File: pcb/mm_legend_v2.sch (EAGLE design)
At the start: 74 parts, among them IC1 ULN2003AD, IC2 TB6612FNG

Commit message: pcb: created pcb design.
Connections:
- net +5V/1 renamed 3V3
- net +5V/2 renamed AVDD
- removed net N$26: IC2.AO1@2
- removed net N$27: IC2.AO2@1, MOTOR1.5
- removed net N$29: IC2.BO1@1, MOTOR2.6
- net IR_DIAG_L: now also IC1.I2, STM1PORT_C_L.PC05; no longer IC1.I4, STM1PORT_C_L.PC03
- net IR_DIAG_R: now also IC1.I5, STM1PORT_C_L.PC01; no longer IC1.I3, STM1PORT_C_L.PC02
- net IR_FRONT_L: now also IC1.I1, STM1PORT_C_L.PC04; no longer IC1.I2, STM1PORT_C_L.PC01
- net IR_FRONT_R: now also IC1.I6; no longer IC1.I1
- net IR_SIDE_L: now also IC1.I3, STM1PORT_C_L.PC03; no longer IC1.I6, STM1PORT_C_L.PC05
- net IR_SIDE_R: now also IC1.I4, STM1PORT_C_L.PC02; no longer IC1.I5, STM1PORT_C_L.PC04
- net MOTOR1_CH1: now also STM1PORT_C_L.PC07; no longer STM1PORT_C_L.PC06
- net MOTOR1_CH2: now also STM1PORT_C_L.PC06; no longer STM1PORT_C_L.PC07
- net MOTOR1_PWM: now also STM1PORT_A_L.PA01; no longer STM1PORT_A_L.PA00
- net MOTOR2_PWM: now also STM1PORT_A_L.PA00; no longer STM1PORT_A_L.PA01
- net N$10: now also IR_DIAG_L.C, R11.2; no longer IR_SIDE_R.C, R14.2
- net N$11: now also IR_SIDE_L.C, R12.2; no longer IR_DIAG_L.C, R13.2
- net N$12: now also IR_SIDE_R.C, R13.2; no longer IR_DIAG_R.C, R12.2
- net N$13: now also IR_DIAG_R.C, R14.2; no longer IR_FRONT_L.C, R11.2
- net N$14: now also R15.2; no longer R10.2
- net N$23: now also IC2.AO1@2, MOTOR1.5; no longer MOTOR1.6
- net N$24: now also IC2.AO2@1, MOTOR1.6
- net N$28: now also IC2.BO1@1, MOTOR2.6
- net N$8: now also IR_FRONT_L.C, R10.2; no longer IR_SIDE_L.C, R15.2
- net PHOTO_DIAG_L: now also STM1PORT_A_L.PA06; no longer STM1PORT_A_L.PA05
- net PHOTO_DIAG_R: now also STM1PORT_A_L.PA03; no longer STM1PORT_A_L.PA04
- net PHOTO_FRONT_L: now also STM1PORT_A_L.PA07; no longer STM1PORT_A_L.PA03
- net PHOTO_SIDE_L: now also STM1PORT_A_L.PA05; no longer STM1PORT_A_L.PA07
- net PHOTO_SIDE_R: now also STM1PORT_A_L.PA04; no longer STM1PORT_A_L.PA06
- net SW1: now also STM1PORT_B_L.PB01; no longer STM1PORT_C_H.PC10
- net SW2: now also STM1PORT_B_L.PB02; no longer STM1PORT_C_H.PC11
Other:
- moved on the sheet: IR_DIAG_L, IR_DIAG_R, IR_FRONT_L, IR_FRONT_R, IR_SIDE_L, IR_SIDE_R

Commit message: pcb: minor changes in pcb and schematic.
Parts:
- C17: value 100u -> 100n
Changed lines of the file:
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@@
 <part name="SUPPLY21" library="supply2" deviceset="VCC" device=""/>
 <part name="SUPPLY22" library="supply2" deviceset="+5V/1" device="" value="3V3"/>
-<part name="C17" library="resistor" deviceset="C-EU" device="C0805K" value="100u"/>
+<part name="C17" library="resistor" deviceset="C-EU" device="C0805K" value="100n"/>
 <part name="R17" library="resistor" deviceset="R-EU_" device="R0805W" value="10k"/>
 <part name="SUPPLY23" library="supply2" deviceset="+5V/1" device="" value="3V3"/>

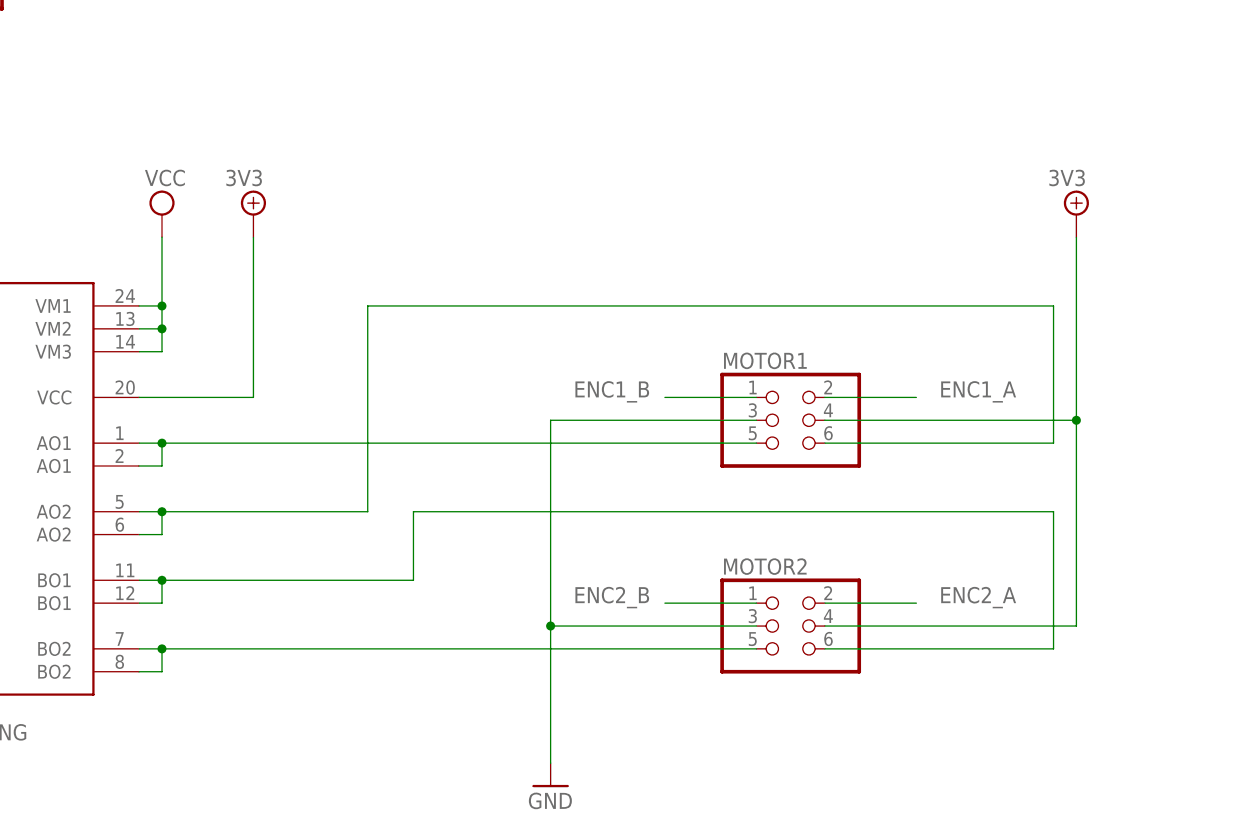
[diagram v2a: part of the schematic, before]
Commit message: pcb: update pcb and schematic.
Changes:
- Moved BT connector away from motor holder.
- Changed pinout of motor connectors - fix issue #1.
- Added thicker lines for motor + and - signals.
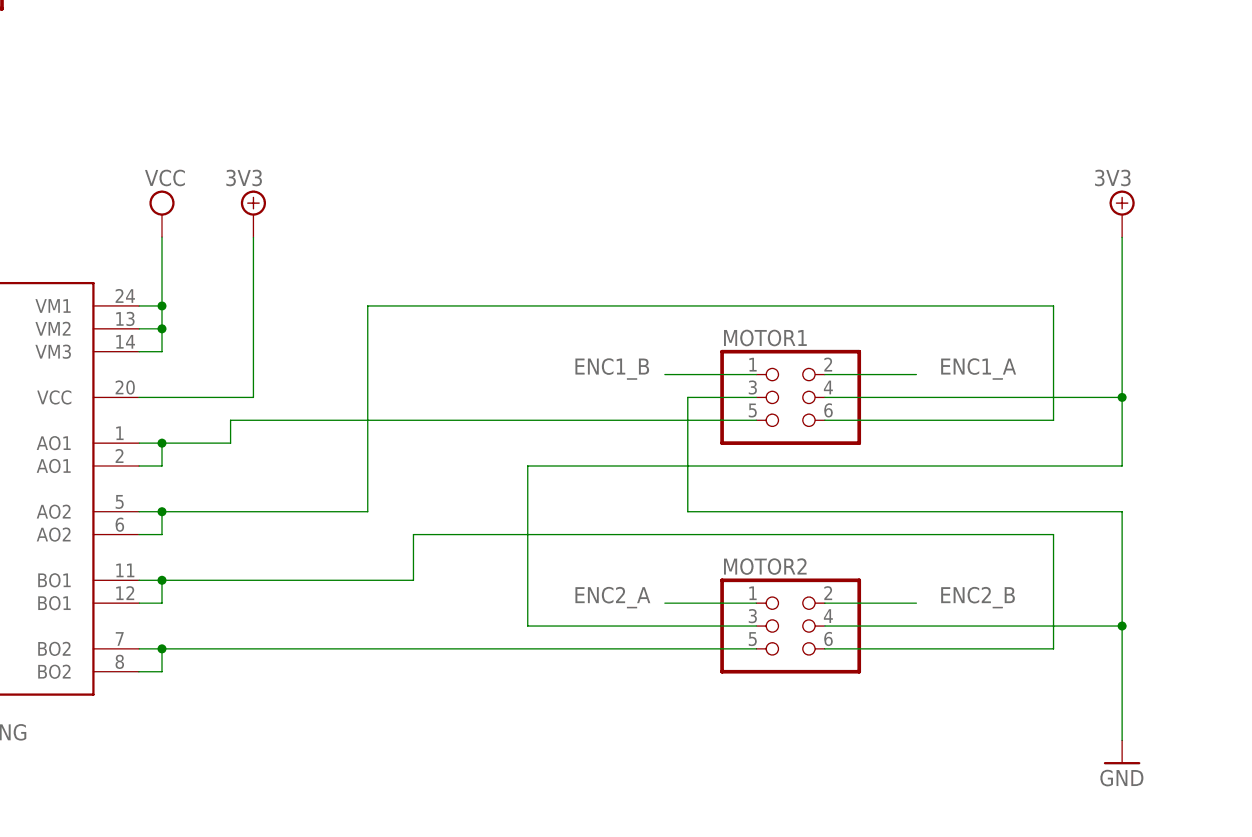
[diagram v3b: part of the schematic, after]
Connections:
- net 3V3: now also MOTOR2.3; no longer MOTOR2.4
- net ENC2_A: now also MOTOR2.1; no longer MOTOR2.2
- net ENC2_B: now also MOTOR2.2; no longer MOTOR2.1
- net GND: now also MOTOR2.4; no longer MOTOR2.3
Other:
- moved on the sheet: MOTOR1
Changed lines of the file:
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@@
 <part name="MOTOR2" library="pinhead" deviceset="PINHD-2X3" device=""/>
 <part name="GND25" library="supply1" deviceset="GND" device=""/>
-<part name="SUPPLY26" library="supply2" deviceset="+5V/1" device="" value="3V3"/>
 <part name="PHOTO_FRONT_R" library="photo_transistor_5mm" deviceset="PHOTO_TRANSISTOR_5MM" device="" value=""/>
 <part name="PHOTO_FRONT_L" library="photo_transistor_5mm" deviceset="PHOTO_TRANSISTOR_5MM" device="" value=""/>
@@
 <part name="SUPPLY31" library="supply2" deviceset="+5V/2" device="" value="AVDD"/>
 <part name="SUPPLY32" library="supply2" deviceset="+5V/2" device="" value="AVDD"/>
+<part name="SUPPLY26" library="supply2" deviceset="+5V/1" device="" value="3V3"/>
 </parts>
 <sheets>
@@
 <instance part="SUPPLY25" gate="G$1" x="208.28" y="-22.86"/>
 <instance part="GND24" gate="1" x="208.28" y="-45.72"/>
-<instance part="MOTOR1" gate="A" x="337.82" y="-5.08"/>
+<instance part="MOTOR1" gate="A" x="337.82" y="-2.54"/>
 <instance part="MOTOR2" gate="A" x="337.82" y="-27.94"/>
-<instance part="GND25" gate="1" x="312.42" y="-45.72"/>
-<instance part="SUPPLY26" gate="G$1" x="370.84" y="17.78"/>
+<instance part="GND25" gate="1" x="375.92" y="-43.18"/>
 <instance part="PHOTO_FRONT_R" gate="G$1" x="190.5" y="144.78"/>
 <instance part="PHOTO_FRONT_L" gate="G$1" x="226.06" y="144.78"/>
@@
 <instance part="SUPPLY31" gate="G$1" x="330.2" y="157.48"/>
 <instance part="SUPPLY32" gate="G$1" x="365.76" y="157.48"/>
+<instance part="SUPPLY26" gate="G$1" x="375.92" y="17.78"/>
 </instances>
 <busses>
@@
 </segment>
 <segment>
-<pinref part="GND25" gate="1" pin="GND"/>
-<wire x1="312.42" y1="-43.18" x2="312.42" y2="-27.94" width="0.1524" layer="91"/>
-<pinref part="MOTOR2" gate="A" pin="3"/>
-<wire x1="312.42" y1="-27.94" x2="335.28" y2="-27.94" width="0.1524" layer="91"/>
-<wire x1="312.42" y1="-27.94" x2="312.42" y2="-5.08" width="0.1524" layer="91"/>
-<pinref part="MOTOR1" gate="A" pin="3"/>
-<wire x1="312.42" y1="-5.08" x2="335.28" y2="-5.08" width="0.1524" layer="91"/>
-<junction x="312.42" y="-27.94"/>
-</segment>
-<segment>
 <pinref part="GND26" gate="1" pin="GND"/>
 <pinref part="R18" gate="G$1" pin="1"/>
@@
 <pinref part="R23" gate="G$1" pin="1"/>
 <wire x1="365.76" y1="119.38" x2="365.76" y2="124.46" width="0.1524" layer="91"/>
+</segment>
+<segment>
+<pinref part="MOTOR2" gate="A" pin="4"/>
+<pinref part="GND25" gate="1" pin="GND"/>
+<wire x1="342.9" y1="-27.94" x2="375.92" y2="-27.94" width="0.1524" layer="91"/>
+<wire x1="375.92" y1="-27.94" x2="375.92" y2="-40.64" width="0.1524" layer="91"/>
+<wire x1="375.92" y1="-27.94" x2="375.92" y2="-15.24" width="0.1524" layer="91"/>
+<wire x1="375.92" y1="-15.24" x2="327.66" y2="-15.24" width="0.1524" layer="91"/>
+<wire x1="327.66" y1="-15.24" x2="327.66" y2="-2.54" width="0.1524" layer="91"/>
+<pinref part="MOTOR1" gate="A" pin="3"/>
+<wire x1="327.66" y1="-2.54" x2="335.28" y2="-2.54" width="0.1524" layer="91"/>
+<junction x="375.92" y="-27.94"/>
 </segment>
 </net>
@@
 <segment>
 <pinref part="SUPPLY26" gate="G$1" pin="+5V/1"/>
-<wire x1="370.84" y1="15.24" x2="370.84" y2="-5.08" width="0.1524" layer="91"/>
+<wire x1="375.92" y1="15.24" x2="375.92" y2="-2.54" width="0.1524" layer="91"/>
 <pinref part="MOTOR1" gate="A" pin="4"/>
-<wire x1="370.84" y1="-5.08" x2="342.9" y2="-5.08" width="0.1524" layer="91"/>
-<wire x1="370.84" y1="-5.08" x2="370.84" y2="-27.94" width="0.1524" layer="91"/>
-<pinref part="MOTOR2" gate="A" pin="4"/>
-<wire x1="370.84" y1="-27.94" x2="342.9" y2="-27.94" width="0.1524" layer="91"/>
-<junction x="370.84" y="-5.08"/>
+<wire x1="375.92" y1="-2.54" x2="342.9" y2="-2.54" width="0.1524" layer="91"/>
+<pinref part="MOTOR2" gate="A" pin="3"/>
+<wire x1="335.28" y1="-27.94" x2="309.88" y2="-27.94" width="0.1524" layer="91"/>
+<wire x1="309.88" y1="-27.94" x2="309.88" y2="-10.16" width="0.1524" layer="91"/>
+<wire x1="309.88" y1="-10.16" x2="375.92" y2="-10.16" width="0.1524" layer="91"/>
+<wire x1="375.92" y1="-10.16" x2="375.92" y2="-2.54" width="0.1524" layer="91"/>
+<junction x="375.92" y="-2.54"/>
 </segment>
 </net>
@@
 <segment>
 <pinref part="MOTOR1" gate="A" pin="1"/>
-<wire x1="335.28" y1="-2.54" x2="325.12" y2="-2.54" width="0.1524" layer="91"/>
-<label x="314.96" y="-2.54" size="1.778" layer="95"/>
+<wire x1="335.28" y1="0" x2="325.12" y2="0" width="0.1524" layer="91"/>
+<label x="314.96" y="0" size="1.778" layer="95"/>
 </segment>
 <segment>
@@
 <segment>
 <pinref part="MOTOR1" gate="A" pin="2"/>
-<wire x1="342.9" y1="-2.54" x2="353.06" y2="-2.54" width="0.1524" layer="91"/>
-<label x="355.6" y="-2.54" size="1.778" layer="95"/>
+<wire x1="342.9" y1="0" x2="353.06" y2="0" width="0.1524" layer="91"/>
+<label x="355.6" y="0" size="1.778" layer="95"/>
 </segment>
 <segment>
@@
 <net name="ENC2_B" class="0">
 <segment>
+<pinref part="STM1" gate="PORT_B_L" pin="PB07"/>
+<wire x1="129.54" y1="63.5" x2="137.16" y2="63.5" width="0.1524" layer="91"/>
+<label x="139.7" y="63.5" size="1.778" layer="95"/>
+</segment>
+<segment>
+<pinref part="MOTOR2" gate="A" pin="2"/>
+<wire x1="342.9" y1="-25.4" x2="353.06" y2="-25.4" width="0.1524" layer="91"/>
+<label x="355.6" y="-25.4" size="1.778" layer="95"/>
+</segment>
+</net>
+<net name="ENC2_A" class="0">
+<segment>
+<pinref part="STM1" gate="PORT_B_L" pin="PB06"/>
+<wire x1="129.54" y1="66.04" x2="137.16" y2="66.04" width="0.1524" layer="91"/>
+<label x="139.7" y="66.04" size="1.778" layer="95"/>
+</segment>
+<segment>
 <pinref part="MOTOR2" gate="A" pin="1"/>
 <wire x1="335.28" y1="-25.4" x2="325.12" y2="-25.4" width="0.1524" layer="91"/>
 <label x="314.96" y="-25.4" size="1.778" layer="95"/>
-</segment>
-<segment>
-<pinref part="STM1" gate="PORT_B_L" pin="PB07"/>
-<wire x1="129.54" y1="63.5" x2="137.16" y2="63.5" width="0.1524" layer="91"/>
-<label x="139.7" y="63.5" size="1.778" layer="95"/>
-</segment>
-</net>
-<net name="ENC2_A" class="0">
-<segment>
-<pinref part="MOTOR2" gate="A" pin="2"/>
-<wire x1="342.9" y1="-25.4" x2="353.06" y2="-25.4" width="0.1524" layer="91"/>
-<label x="355.6" y="-25.4" size="1.778" layer="95"/>
-</segment>
-<segment>
-<pinref part="STM1" gate="PORT_B_L" pin="PB06"/>
-<wire x1="129.54" y1="66.04" x2="137.16" y2="66.04" width="0.1524" layer="91"/>
-<label x="139.7" y="66.04" size="1.778" layer="95"/>
 </segment>
 </net>
@@
 <wire x1="292.1" y1="-15.24" x2="292.1" y2="7.62" width="0.1524" layer="91"/>
 <pinref part="MOTOR1" gate="A" pin="6"/>
-<wire x1="368.3" y1="7.62" x2="368.3" y2="-7.62" width="0.1524" layer="91"/>
-<wire x1="368.3" y1="-7.62" x2="342.9" y2="-7.62" width="0.1524" layer="91"/>
+<wire x1="368.3" y1="7.62" x2="368.3" y2="-5.08" width="0.1524" layer="91"/>
+<wire x1="368.3" y1="-5.08" x2="342.9" y2="-5.08" width="0.1524" layer="91"/>
 <wire x1="292.1" y1="7.62" x2="368.3" y2="7.62" width="0.1524" layer="91"/>
 </segment>
@@
 <wire x1="266.7" y1="-22.86" x2="269.24" y2="-22.86" width="0.1524" layer="91"/>
 <wire x1="269.24" y1="-22.86" x2="297.18" y2="-22.86" width="0.1524" layer="91"/>
-<wire x1="297.18" y1="-22.86" x2="297.18" y2="-15.24" width="0.1524" layer="91"/>
-<wire x1="297.18" y1="-15.24" x2="368.3" y2="-15.24" width="0.1524" layer="91"/>
-<wire x1="368.3" y1="-15.24" x2="368.3" y2="-30.48" width="0.1524" layer="91"/>
+<wire x1="297.18" y1="-22.86" x2="297.18" y2="-17.78" width="0.1524" layer="91"/>
+<wire x1="297.18" y1="-17.78" x2="368.3" y2="-17.78" width="0.1524" layer="91"/>
+<wire x1="368.3" y1="-17.78" x2="368.3" y2="-30.48" width="0.1524" layer="91"/>
 <pinref part="MOTOR2" gate="A" pin="6"/>
 <wire x1="368.3" y1="-30.48" x2="342.9" y2="-30.48" width="0.1524" layer="91"/>
@@
 <pinref part="IC2" gate="G$1" pin="AO1@1"/>
 <wire x1="266.7" y1="-7.62" x2="269.24" y2="-7.62" width="0.1524" layer="91"/>
-<junction x="269.24" y="-7.62"/>
 <wire x1="269.24" y1="-10.16" x2="269.24" y2="-7.62" width="0.1524" layer="91"/>
 <pinref part="IC2" gate="G$1" pin="AO1@2"/>
 <wire x1="266.7" y1="-10.16" x2="269.24" y2="-10.16" width="0.1524" layer="91"/>
 <pinref part="MOTOR1" gate="A" pin="5"/>
-<wire x1="335.28" y1="-7.62" x2="269.24" y2="-7.62" width="0.1524" layer="91"/>
-</segment>
-</net>
+<wire x1="335.28" y1="-5.08" x2="276.86" y2="-5.08" width="0.1524" layer="91"/>
+<wire x1="276.86" y1="-5.08" x2="276.86" y2="-7.62" width="0.1524" layer="91"/>
+<wire x1="276.86" y1="-7.62" x2="269.24" y2="-7.62" width="0.1524" layer="91"/>
+<junction x="269.24" y="-7.62"/>
+</segment>
+</net>

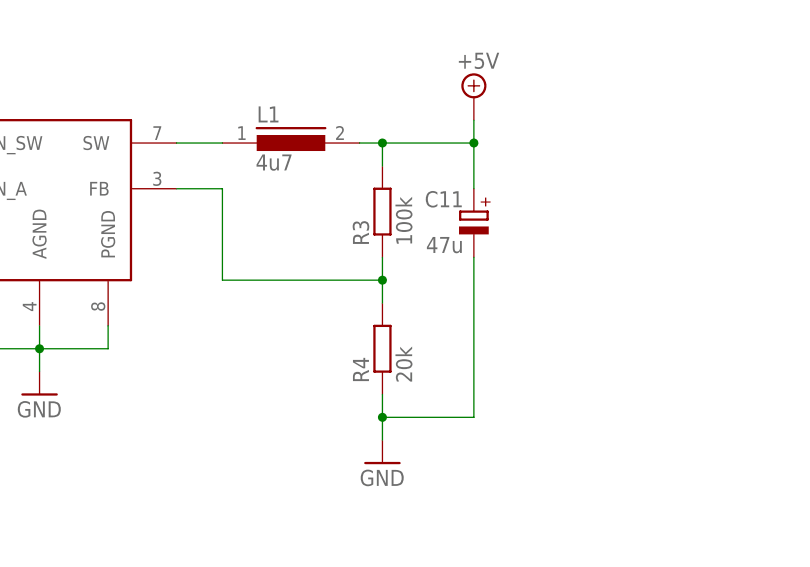
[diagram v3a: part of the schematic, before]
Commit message: pcb: updated vbat resistors to real values.
Until now resistor values were 20k and 100k. 20k resistor doesn't exist in the series.
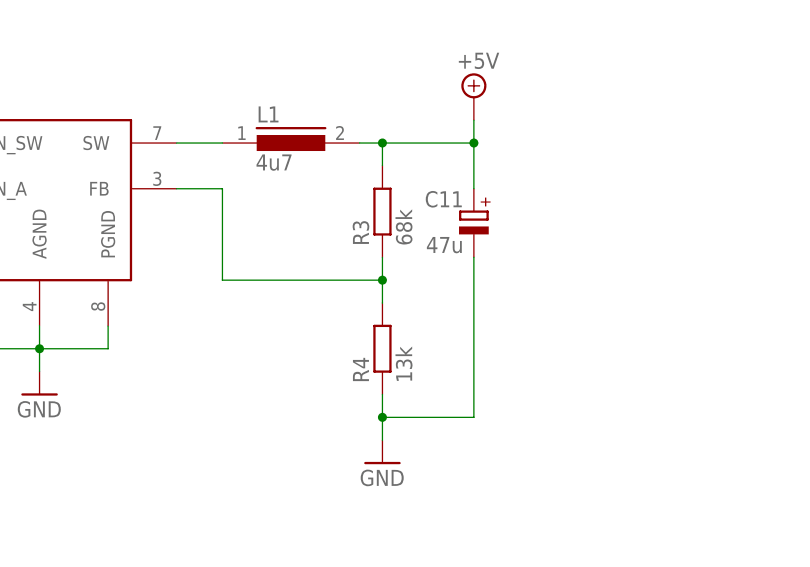
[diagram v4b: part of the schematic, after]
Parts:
- R3: value 100k -> 68k
- R4: value 20k -> 13k
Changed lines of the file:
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@@
 <part name="SUPPLY5" library="supply2" deviceset="VCC" device=""/>
 <part name="L1" library="inductors" deviceset="DR74" device="" value="4u7"/>
-<part name="R3" library="resistor" deviceset="R-EU_" device="R0805W" value="100k"/>
-<part name="R4" library="resistor" deviceset="R-EU_" device="R0805W" value="20k"/>
+<part name="R3" library="resistor" deviceset="R-EU_" device="R0805W" value="68k"/>
+<part name="R4" library="resistor" deviceset="R-EU_" device="R0805W" value="13k"/>
 <part name="C11" library="resistor" deviceset="CPOL-EU" device="B/3528-21W" value="47u"/>
 <part name="GND10" library="supply1" deviceset="GND" device=""/>
